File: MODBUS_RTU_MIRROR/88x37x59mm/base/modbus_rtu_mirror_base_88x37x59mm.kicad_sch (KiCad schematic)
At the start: 3 parts, among them J1 Conn_01x01_Male, J2 Conn_01x02_Female

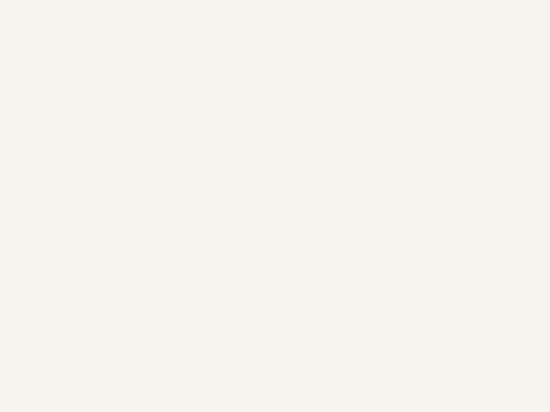
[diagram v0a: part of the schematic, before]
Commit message: added RS485 terminals
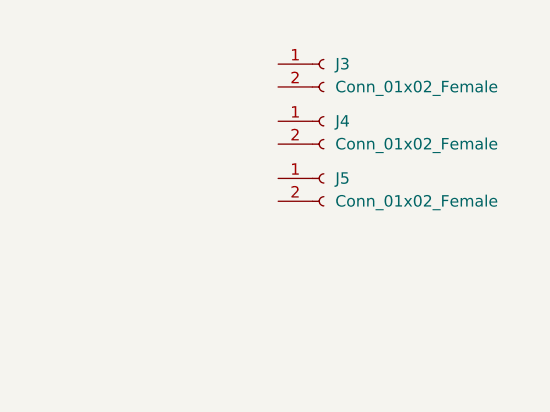
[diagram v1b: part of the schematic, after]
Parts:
- added J3, J4, J5: Conn_01x02_Female, TerminalBlock_RND:TerminalBlock_RND_205-00012_1x02_P5.00mm_Horizontal, symbol Connector:Conn_01x02_Female
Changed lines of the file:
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@@
     (stroke (width 0) (type default) (color 0 0 0 0))
+  )
+  (symbol (lib_id "Connector:Conn_01x02_Female") (at 213.36 90.17 0) (unit 1)
+    (in_bom yes) (on_board yes) (fields_autoplaced)
+    (property "Reference" "J5" (id 0) (at 214.63 90.1699 0)
+      (effects (font (size 1.27 1.27)) (justify left))
+    )
+    (property "Value" "Conn_01x02_Female" (id 1) (at 214.63 92.7099 0)
+      (effects (font (size 1.27 1.27)) (justify left))
+    )
+    (property "Footprint" "TerminalBlock_RND:TerminalBlock_RND_205-00012_1x02_P5.00mm_Horizontal" (id 2) (at 213.36 90.17 0)
+      (effects (font (size 1.27 1.27)) hide)
+    )
+    (property "Datasheet" "~" (id 3) (at 213.36 90.17 0)
+      (effects (font (size 1.27 1.27)) hide)
+    )
+    (pin "1")
+    (pin "2")
   )
   (symbol (lib_id "power:GND") (at 115.57 111.76 0) (unit 1)
@@
     (pin "4")
   )
+  (symbol (lib_id "Connector:Conn_01x02_Female") (at 213.36 77.47 0) (unit 1)
+    (in_bom yes) (on_board yes) (fields_autoplaced)
+    (property "Reference" "J3" (id 0) (at 214.63 77.4699 0)
+      (effects (font (size 1.27 1.27)) (justify left))
+    )
+    (property "Value" "Conn_01x02_Female" (id 1) (at 214.63 80.0099 0)
+      (effects (font (size 1.27 1.27)) (justify left))
+    )
+    (property "Footprint" "TerminalBlock_RND:TerminalBlock_RND_205-00012_1x02_P5.00mm_Horizontal" (id 2) (at 213.36 77.47 0)
+      (effects (font (size 1.27 1.27)) hide)
+    )
+    (property "Datasheet" "~" (id 3) (at 213.36 77.47 0)
+      (effects (font (size 1.27 1.27)) hide)
+    )
+    (pin "1")
+    (pin "2")
+  )
   (symbol (lib_id "Connector:Conn_01x02_Female") (at 113.03 81.28 0) (mirror y) (unit 1)
     (in_bom yes) (on_board yes) (fields_autoplaced)
@@
     )
     (property "Datasheet" "~" (id 3) (at 113.03 81.28 0)
+      (effects (font (size 1.27 1.27)) hide)
+    )
+    (pin "1")
+    (pin "2")
+  )
+  (symbol (lib_id "Connector:Conn_01x02_Female") (at 213.36 83.82 0) (unit 1)
+    (in_bom yes) (on_board yes) (fields_autoplaced)
+    (property "Reference" "J4" (id 0) (at 214.63 83.8199 0)
+      (effects (font (size 1.27 1.27)) (justify left))
+    )
+    (property "Value" "Conn_01x02_Female" (id 1) (at 214.63 86.3599 0)
+      (effects (font (size 1.27 1.27)) (justify left))
+    )
+    (property "Footprint" "TerminalBlock_RND:TerminalBlock_RND_205-00012_1x02_P5.00mm_Horizontal" (id 2) (at 213.36 83.82 0)
+      (effects (font (size 1.27 1.27)) hide)
+    )
+    (property "Datasheet" "~" (id 3) (at 213.36 83.82 0)
       (effects (font (size 1.27 1.27)) hide)
     )
@@
       (reference "J2") (unit 1) (value "Conn_01x02_Female") (footprint "TerminalBlock_RND:TerminalBlock_RND_205-00012_1x02_P5.00mm_Horizontal")
     )
+    (path "/5ced11a0-0d47-4e79-9e6a-b2ebd3d34a8b"
+      (reference "J3") (unit 1) (value "Conn_01x02_Female") (footprint "TerminalBlock_RND:TerminalBlock_RND_205-00012_1x02_P5.00mm_Horizontal")
+    )
+    (path "/7fe35ed1-4d27-4eeb-bd14-16529ba82968"
+      (reference "J4") (unit 1) (value "Conn_01x02_Female") (footprint "TerminalBlock_RND:TerminalBlock_RND_205-00012_1x02_P5.00mm_Horizontal")
+    )
+    (path "/02ff2782-1767-4d24-9ec8-5ee83313e741"
+      (reference "J5") (unit 1) (value "Conn_01x02_Female") (footprint "TerminalBlock_RND:TerminalBlock_RND_205-00012_1x02_P5.00mm_Horizontal")
+    )
     (path "/38b4545f-3eb4-46ed-9068-4cd25c6f82b9"

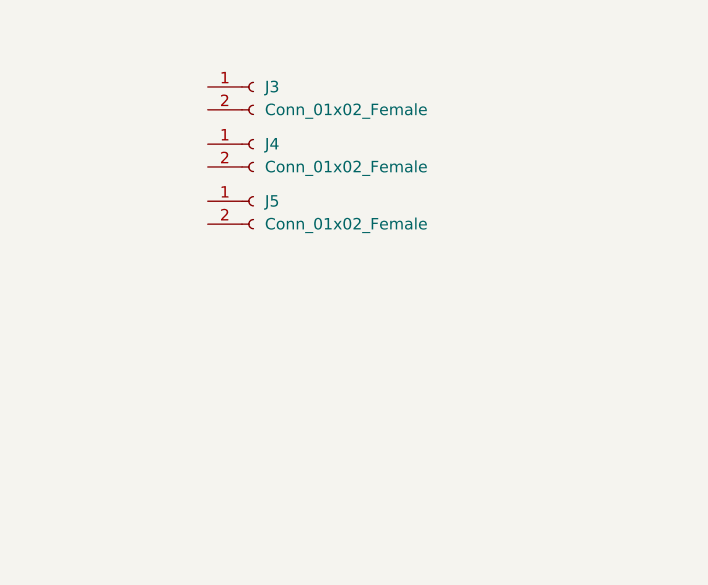
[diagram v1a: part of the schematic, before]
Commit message: addes 2x rs485 chip
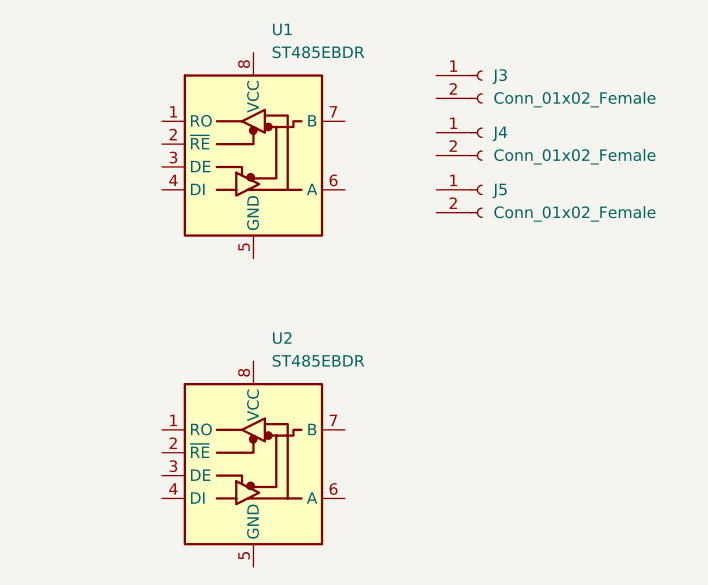
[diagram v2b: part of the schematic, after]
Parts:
- added U1, U2: ST485EBDR, Package_SO:SOIC-8_3.9x4.9mm_P1.27mm, symbol Interface_UART:ST485EBDR
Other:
- moved on the sheet: J3, J4, J5
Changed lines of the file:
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@@
     (stroke (width 0) (type default) (color 0 0 0 0))
   )
-  (symbol (lib_id "Connector:Conn_01x02_Female") (at 213.36 90.17 0) (unit 1)
+  (symbol (lib_id "Connector:Conn_01x02_Female") (at 238.76 88.9 0) (unit 1)
     (in_bom yes) (on_board yes) (fields_autoplaced)
-    (property "Reference" "J5" (id 0) (at 214.63 90.1699 0)
+    (property "Reference" "J5" (id 0) (at 240.03 88.8999 0)
       (effects (font (size 1.27 1.27)) (justify left))
     )
-    (property "Value" "Conn_01x02_Female" (id 1) (at 214.63 92.7099 0)
+    (property "Value" "Conn_01x02_Female" (id 1) (at 240.03 91.4399 0)
       (effects (font (size 1.27 1.27)) (justify left))
     )
-    (property "Footprint" "TerminalBlock_RND:TerminalBlock_RND_205-00012_1x02_P5.00mm_Horizontal" (id 2) (at 213.36 90.17 0)
+    (property "Footprint" "TerminalBlock_RND:TerminalBlock_RND_205-00012_1x02_P5.00mm_Horizontal" (id 2) (at 238.76 88.9 0)
       (effects (font (size 1.27 1.27)) hide)
     )
-    (property "Datasheet" "~" (id 3) (at 213.36 90.17 0)
+    (property "Datasheet" "~" (id 3) (at 238.76 88.9 0)
       (effects (font (size 1.27 1.27)) hide)
     )
@@
     (pin "4")
   )
-  (symbol (lib_id "Connector:Conn_01x02_Female") (at 213.36 77.47 0) (unit 1)
+  (symbol (lib_id "Interface_UART:ST485EBDR") (at 213.36 83.82 0) (unit 1)
     (in_bom yes) (on_board yes) (fields_autoplaced)
-    (property "Reference" "J3" (id 0) (at 214.63 77.4699 0)
+    (property "Reference" "U1" (id 0) (at 215.3794 71.12 0)
       (effects (font (size 1.27 1.27)) (justify left))
     )
-    (property "Value" "Conn_01x02_Female" (id 1) (at 214.63 80.0099 0)
+    (property "Value" "ST485EBDR" (id 1) (at 215.3794 73.66 0)
       (effects (font (size 1.27 1.27)) (justify left))
     )
-    (property "Footprint" "TerminalBlock_RND:TerminalBlock_RND_205-00012_1x02_P5.00mm_Horizontal" (id 2) (at 213.36 77.47 0)
+    (property "Footprint" "Package_SO:SOIC-8_3.9x4.9mm_P1.27mm" (id 2) (at 213.36 106.68 0)
       (effects (font (size 1.27 1.27)) hide)
     )
-    (property "Datasheet" "~" (id 3) (at 213.36 77.47 0)
+    (property "Datasheet" "http://www.st.com/resource/en/datasheet/st485eb.pdf" (id 3) (at 213.36 82.55 0)
+      (effects (font (size 1.27 1.27)) hide)
+    )
+    (pin "1")
+    (pin "2")
+    (pin "3")
+    (pin "4")
+    (pin "5")
+    (pin "6")
+    (pin "7")
+    (pin "8")
+  )
+  (symbol (lib_id "Connector:Conn_01x02_Female") (at 238.76 76.2 0) (unit 1)
+    (in_bom yes) (on_board yes) (fields_autoplaced)
+    (property "Reference" "J3" (id 0) (at 240.03 76.1999 0)
+      (effects (font (size 1.27 1.27)) (justify left))
+    )
+    (property "Value" "Conn_01x02_Female" (id 1) (at 240.03 78.7399 0)
+      (effects (font (size 1.27 1.27)) (justify left))
+    )
+    (property "Footprint" "TerminalBlock_RND:TerminalBlock_RND_205-00012_1x02_P5.00mm_Horizontal" (id 2) (at 238.76 76.2 0)
+      (effects (font (size 1.27 1.27)) hide)
+    )
+    (property "Datasheet" "~" (id 3) (at 238.76 76.2 0)
       (effects (font (size 1.27 1.27)) hide)
     )
@@
     (pin "2")
   )
-  (symbol (lib_id "Connector:Conn_01x02_Female") (at 213.36 83.82 0) (unit 1)
+  (symbol (lib_id "Connector:Conn_01x02_Female") (at 238.76 82.55 0) (unit 1)
     (in_bom yes) (on_board yes) (fields_autoplaced)
-    (property "Reference" "J4" (id 0) (at 214.63 83.8199 0)
+    (property "Reference" "J4" (id 0) (at 240.03 82.5499 0)
       (effects (font (size 1.27 1.27)) (justify left))
     )
-    (property "Value" "Conn_01x02_Female" (id 1) (at 214.63 86.3599 0)
+    (property "Value" "Conn_01x02_Female" (id 1) (at 240.03 85.0899 0)
       (effects (font (size 1.27 1.27)) (justify left))
     )
-    (property "Footprint" "TerminalBlock_RND:TerminalBlock_RND_205-00012_1x02_P5.00mm_Horizontal" (id 2) (at 213.36 83.82 0)
+    (property "Footprint" "TerminalBlock_RND:TerminalBlock_RND_205-00012_1x02_P5.00mm_Horizontal" (id 2) (at 238.76 82.55 0)
       (effects (font (size 1.27 1.27)) hide)
     )
-    (property "Datasheet" "~" (id 3) (at 213.36 83.82 0)
+    (property "Datasheet" "~" (id 3) (at 238.76 82.55 0)
       (effects (font (size 1.27 1.27)) hide)
     )
@@
     )
     (pin "1")
+  )
+  (symbol (lib_id "Interface_UART:ST485EBDR") (at 213.36 118.11 0) (unit 1)
+    (in_bom yes) (on_board yes) (fields_autoplaced)
+    (property "Reference" "U2" (id 0) (at 215.3794 105.41 0)
+      (effects (font (size 1.27 1.27)) (justify left))
+    )
+    (property "Value" "ST485EBDR" (id 1) (at 215.3794 107.95 0)
+      (effects (font (size 1.27 1.27)) (justify left))
+    )
+    (property "Footprint" "Package_SO:SOIC-8_3.9x4.9mm_P1.27mm" (id 2) (at 213.36 140.97 0)
+      (effects (font (size 1.27 1.27)) hide)
+    )
+    (property "Datasheet" "http://www.st.com/resource/en/datasheet/st485eb.pdf" (id 3) (at 213.36 116.84 0)
+      (effects (font (size 1.27 1.27)) hide)
+    )
+    (pin "1")
+    (pin "2")
+    (pin "3")
+    (pin "4")
+    (pin "5")
+    (pin "6")
+    (pin "7")
+    (pin "8")
   )
   (sheet_instances
@@
       (reference "PS1") (unit 1) (value "HLK-PM01") (footprint "Converter_ACDC:Converter_ACDC_HiLink_HLK-PMxx")
     )
+    (path "/463ed642-1279-4aee-8f11-46dfbb8a9924"
+      (reference "U1") (unit 1) (value "ST485EBDR") (footprint "Package_SO:SOIC-8_3.9x4.9mm_P1.27mm")
+    )
+    (path "/d6283d3e-684b-4ba2-9bc3-9a0a822cd582"
+      (reference "U2") (unit 1) (value "ST485EBDR") (footprint "Package_SO:SOIC-8_3.9x4.9mm_P1.27mm")
+    )
   )

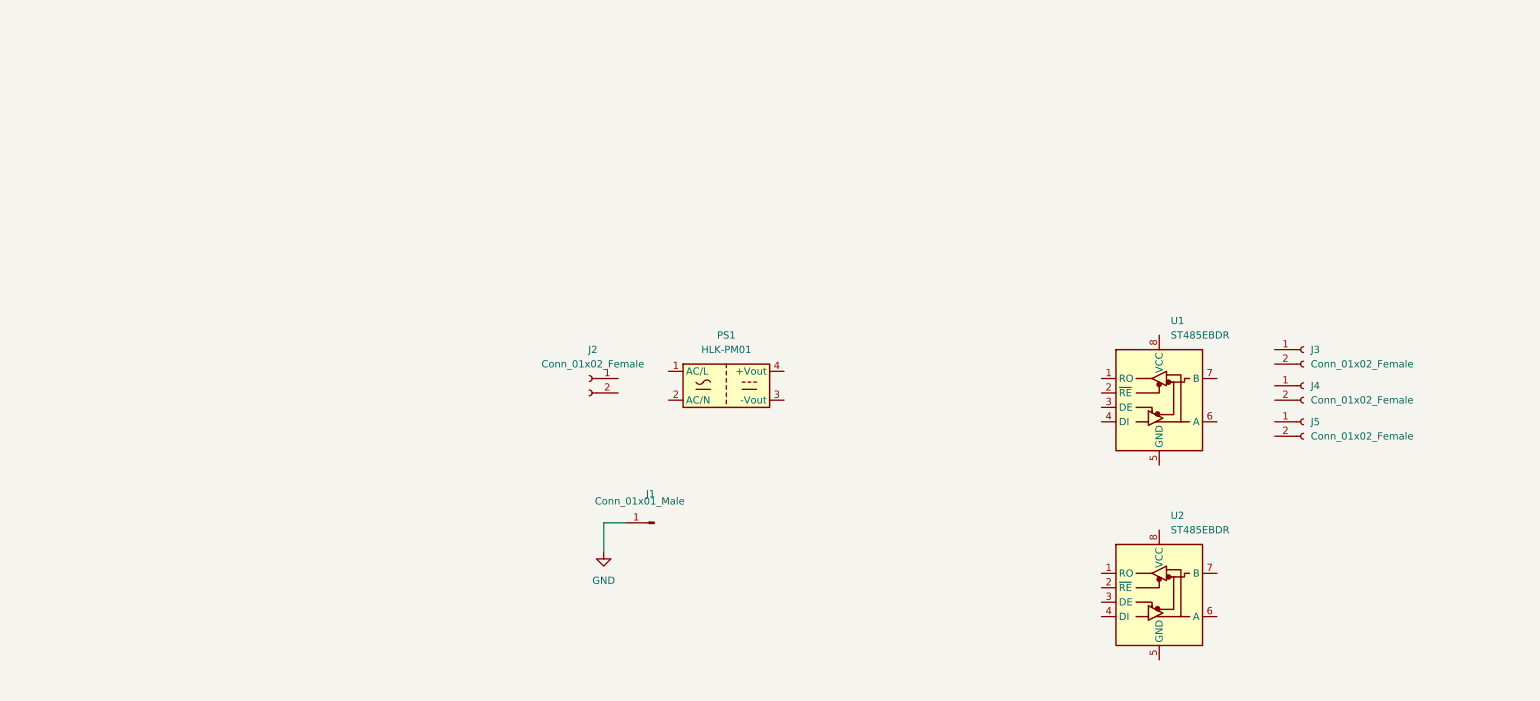
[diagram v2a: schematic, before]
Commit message: all traces routed
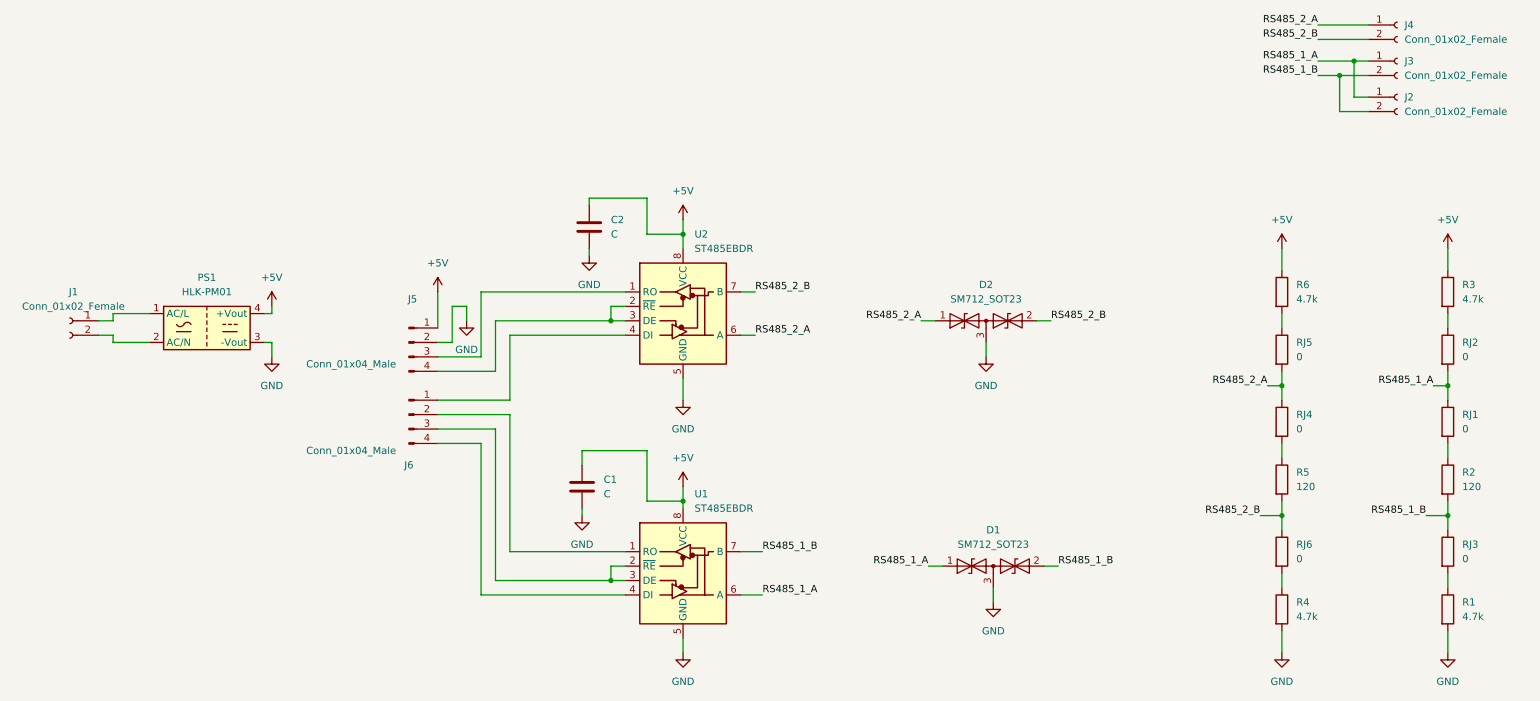
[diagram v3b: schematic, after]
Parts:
- removed J1: Conn_01x01_Male, Connector_PinHeader_2.54mm:PinHeader_1x01_P2.54mm_Vertical, symbol Connector:Conn_01x01_Male
- added C1, C2: C, Capacitor_SMD:C_0805_2012Metric_Pad1.18x1.45mm_HandSolder, symbol Device:C
- added D1, D2: SM712_SOT23, Package_TO_SOT_SMD:SOT-23, symbol Diode:SM712_SOT23
- added J5, J6: Conn_01x04_Male, Connector_PinHeader_2.54mm:PinHeader_1x04_P2.54mm_Vertical, symbol Connector:Conn_01x04_Male
- added R1, R3, R4, R6: 4.7k, Resistor_SMD:R_0805_2012Metric_Pad1.20x1.40mm_HandSolder, symbol Device:R
- added R2, R5: 120, Resistor_SMD:R_0805_2012Metric_Pad1.20x1.40mm_HandSolder, symbol Device:R
- added RJ1, RJ2, RJ3, RJ4, RJ5, RJ6: 0, Resistor_SMD:R_0805_2012Metric_Pad1.20x1.40mm_HandSolder, symbol Device:R
- renumbered J2 to J1, J3 to J2, J4 to J3, J5 to J4, U2 to U1, U1 to U2
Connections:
- net GND: now also PS1.3 (-Vout), U1.5 (GND), U2.5 (GND), C1.2, C2.2, D1.3 (common), D2.3 (common), J5.2 (Pin_2), R1.2, R4.2
- net RS485_2_A: now reaches J4.1 (Pin_1)
- net RS485_2_A: now also U2.6 (A), D2.1 (A1), RJ4.1, RJ5.2
- net RS485_2_B: now reaches J4.2 (Pin_2)
- net RS485_2_B: now also U2.7 (B), D2.2 (A2), R5.2, RJ6.1
- net at PS1.1 (AC/L): now also J1.1 (Pin_1)
- net at PS1.2 (AC/N): now also J1.2 (Pin_2)
- net +5V: now reaches PS1.4 (+Vout)
- net +5V: now also U1.8 (VCC), U2.8 (VCC), C1.1, C2.1, J5.1 (Pin_1), R3.1, R6.1
- net at U2.1 (RO): now also J5.3 (Pin_3)
- net at U2.2 (~{RE}): now also U2.3 (DE), J5.4 (Pin_4)
- net at U2.4 (DI): now also J6.1 (Pin_1)
- net RS485_1_A: now reaches J2.1 (Pin_1)
- net RS485_1_A: now also J3.1 (Pin_1), U1.6 (A), D1.1 (A1), RJ1.1, RJ2.2
- net RS485_1_B: now reaches J2.2 (Pin_2)
- net RS485_1_B: now also J3.2 (Pin_2), U1.7 (B), D1.2 (A2), R2.2, RJ3.1
- net at U1.1 (RO): now also J6.2 (Pin_2)
- net at U1.2 (~{RE}): now also U1.3 (DE), J6.3 (Pin_3)
- net at U1.4 (DI): now also J6.4 (Pin_4)
- new net: R5.1, RJ4.2
- new net: R2.1, RJ1.2
- new net: R1.1, RJ3.2
- new net: R3.2, RJ2.1
- new net: R6.2, RJ5.1
- new net: R4.1, RJ6.2
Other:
- moved on the sheet: J1, J2, J3, J4, PS1, U1, U2

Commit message: all elements placed
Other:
- note added: "To side board"
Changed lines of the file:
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@@
     (stroke (width 0) (type default) (color 0 0 0 0))
+  )
+  (text "To side board" (at 81.28 83.82 0)
+    (effects (font (size 1.27 1.27)) (justify left bottom))
   )
   (label "RS485_1_B" (at 143.51 111.76 0)

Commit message: created folder for different processor version
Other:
- title: (none) -> Modbus RTU mirror base board
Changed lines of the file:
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@@
 (kicad_sch (version 20211123) (generator eeschema)
   (paper "A4")
+  (title_block
+    (title "Modbus RTU mirror base board")
+  )
   (junction (at 234.95 105.41) (diameter 0) (color 0 0 0 0)
   )
